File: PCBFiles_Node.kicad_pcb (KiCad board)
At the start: 2 copper layers, 1 part

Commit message: STM32 IC
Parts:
- removed IC**: QFN50P500X500X60-33N-D, SamacSys_Parts:QFN50P500X500X60-33N-D
- added IC1: STM32L432KCU3, SamacSys_Parts:QFN50P500X500X60-33N-D, F.Cu at (125.5, 23.0)

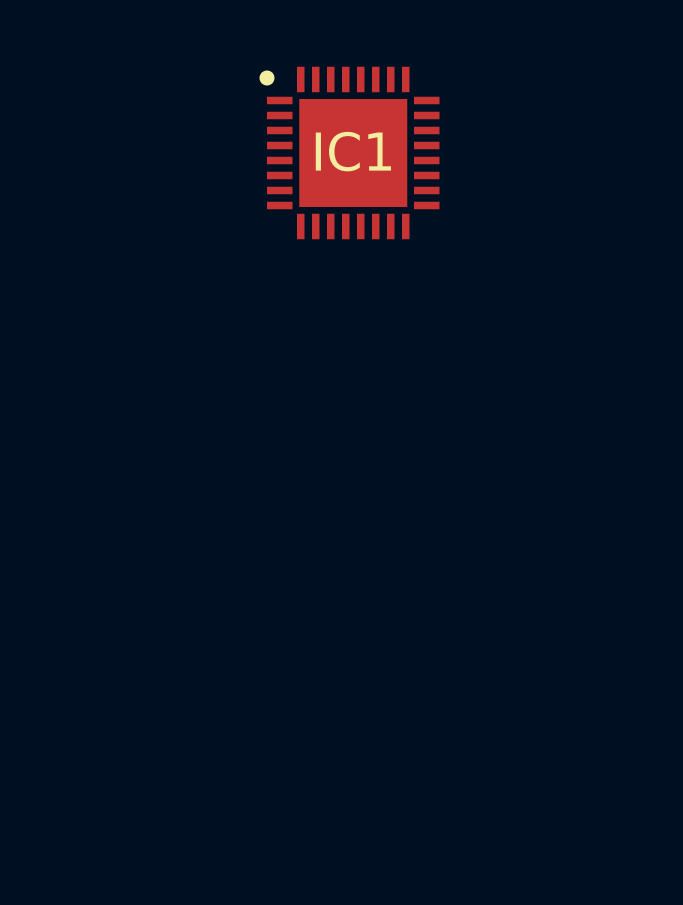
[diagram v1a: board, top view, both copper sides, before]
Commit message: Voltage regulator, Crystal, RFM9x, base settings
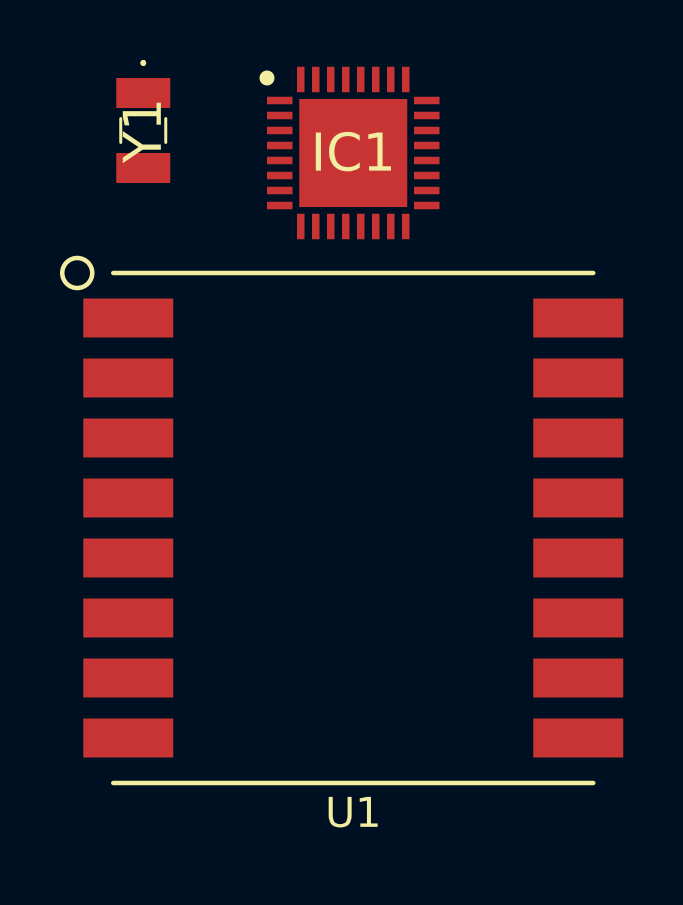
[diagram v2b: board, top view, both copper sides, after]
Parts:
- added U1: RFM9X, LoRa_RFM9x:RFM9X-SMD, F.Cu at (125.5, 35.5)
- added Y1: NX3215SA-32.768K-STD-MUS-2, SamacSys_Parts:NX3215SA32768KSTDMUS2, F.Cu at (118.5, 22.2)
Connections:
- IC1 pad 1: unconnected-(IC1-Pad1) -> +3V3
- IC1 pad 16: unconnected-(IC1-Pad16) -> GND
- IC1 pad 17: unconnected-(IC1-Pad17) -> +3V3
- IC1 pad 19: unconnected-(IC1-Pad19) -> I2C1_SCL
- IC1 pad 2: unconnected-(IC1-Pad2) -> HSE_IN
- IC1 pad 20: unconnected-(IC1-Pad20) -> I2C1_SDA
- IC1 pad 21: unconnected-(IC1-Pad21) -> SPI1_MISO
- IC1 pad 22: unconnected-(IC1-Pad22) -> SPI1_MOSI
- IC1 pad 3: unconnected-(IC1-Pad3) -> HSE_OUT
- IC1 pad 32: unconnected-(IC1-Pad32) -> GND
- IC1 pad 33: unconnected-(IC1-Pad33) -> GND
- IC1 pad 5: unconnected-(IC1-Pad5) -> +3.3VA
- IC1 pad 7: unconnected-(IC1-Pad7) -> SPI1_SCK

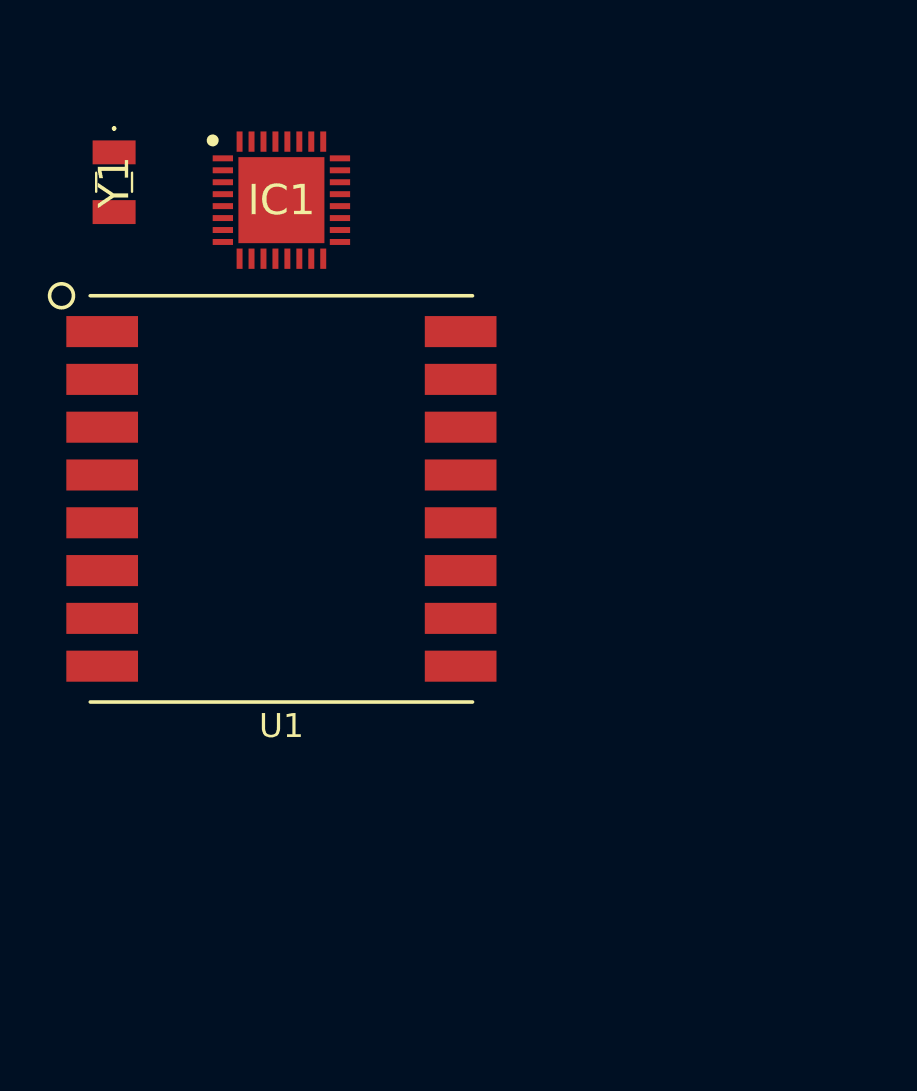
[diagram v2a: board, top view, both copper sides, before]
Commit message: Connectors, MPU Circuit & Pins Schematic Update
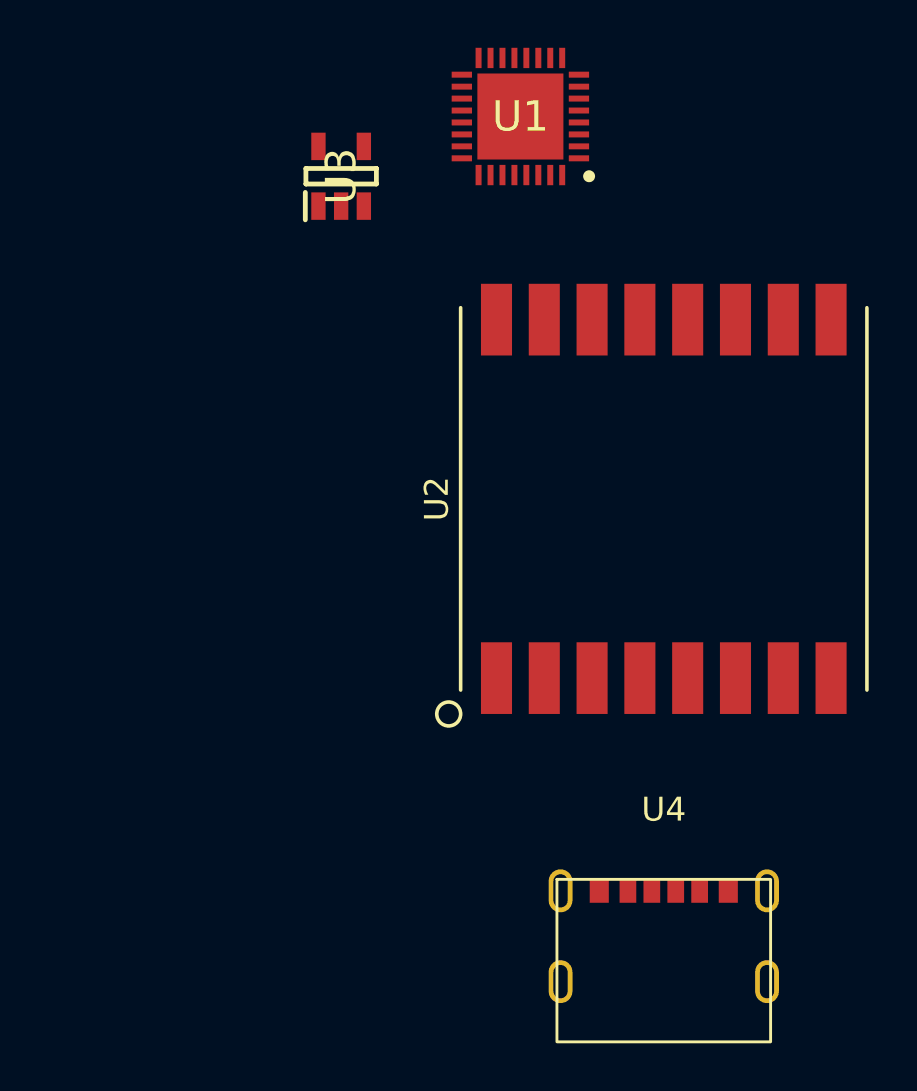
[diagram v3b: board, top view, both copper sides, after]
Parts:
- removed IC1: STM32L432KCU3, SamacSys_Parts:QFN50P500X500X60-33N-D
- removed Y1: NX3215SA-32.768K-STD-MUS-2, SamacSys_Parts:NX3215SA32768KSTDMUS2
- added U2: RFM9X, LoRa_RFM9x:RFM9X-SMD, F.Cu at (141.5, 35.5)
- added U3: STLQ015M33R, SamacSys_Parts:SOT95P280X145-5N, F.Cu at (128.0, 22.0)
- added U4: USB_C_2.0_6PIN, Connector_USB:USB_TYPE_C_2.0_6PIN, F.Cu at (141.5, 49.0)
- U1: value RFM9X -> STM32L432KCU3; footprint LoRa_RFM9x:RFM9X-SMD -> SamacSys_Parts:QFN50P500X500X60-33N-D
- moved U1 18.9 mm to (135.5, 19.5)
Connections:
- net DIO0 renamed V_GAS
- net DIO4 renamed RED_LED
- U1 pad 1: GND -> +3V3
- U1 pad 10: DIO1 -> V_REF_OUT
- U1 pad 12: +3V3 -> RESET_RFM9X
- U1 pad 14: DIO3 -> unconnected-(U1-Pad14)
- U1 pad 15: GND -> unconnected-(U1-Pad15)
- U1 pad 16: /ANT -> GND
- U1 pad 2: SPI1_MISO -> HSE_IN
- U1 pad 3: SPI1_MOSI -> HSE_OUT
- U1 pad 4: SPI1_SCK -> Net-(C1-Pad1)
- U1 pad 5: SPI1_NSS -> +3V3
- U1 pad 6: RESET_RFM9X -> V_REF_IN
- U1 pad 7: DIO5 -> SPI1_SCK
- U1 pad 8: GND -> GREEN_LED
- U1 pad 9: DIO2 -> V_REF_OUT

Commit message: First PCB Design
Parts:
- removed U4: USB_C_2.0_6PIN, Connector_USB:USB_TYPE_C_2.0_6PIN
- added C1: 100n, Capacitor_SMD:C_0402_1005Metric, F.Cu at (124.0, 87.9)
- added C10: 1u, Capacitor_SMD:C_0402_1005Metric, F.Cu at (119.5, 89.7)
- added C11: 10n, Capacitor_SMD:C_0402_1005Metric, F.Cu at (119.0, 88.1)
- added C2: 1u, Capacitor_SMD:C_0402_1005Metric, F.Cu at (124.4, 96.6)
- added C3: 10u, Capacitor_SMD:C_1206_3216Metric, F.Cu at (106.1, 100.2)
- added C4: 100n, Capacitor_SMD:C_0402_1005Metric, F.Cu at (125.6, 96.6)
- added C5: 100n, Capacitor_SMD:C_0402_1005Metric, F.Cu at (126.8, 96.6)
- added C6: 100n, Capacitor_SMD:C_0402_1005Metric, F.Cu at (128.0, 96.6)
- added C7: 10u, Capacitor_SMD:C_1206_3216Metric, F.Cu at (106.7, 87.7)
- added C8: 13p, Capacitor_SMD:C_0402_1005Metric, F.Cu at (114.2, 91.5)
- added C9: 13p, Capacitor_SMD:C_0402_1005Metric, F.Cu at (114.2, 93.6)
- added D1: Green, LED_SMD:LED_0201_0603Metric, F.Cu at (116.5, 96.3)
- added D2: Red, LED_SMD:LED_0201_0603Metric, F.Cu at (120.7, 98.5)
- added H1: MountingHole, MountingHole:MountingHole_2.2mm_M2_Pad_Via, F.Cu at (161.6, 80.4)
- added H2: MountingHole, MountingHole:MountingHole_2.2mm_M2_Pad_Via, F.Cu at (101.6, 101.9)
- added J1: SWD, Connector_PinHeader_2.54mm:PinHeader_2x05_P2.54mm_Vertical_SMD, F.Cu at (133.1, 84.4)
- added J2: SHT31, Connector_PinSocket_2.54mm:PinSocket_1x07_P2.54mm_Vertical, F.Cu at (141.7, 102.8)
- added J3: SPEC Sensor 968-001, Connector_PinHeader_2.54mm:PinHeader_1x08_P2.54mm_Horizontal, B.Cu at (110.1, 97.0)
- added J5: USB_B_Micro, Connector_USB:USB_Micro-B_Molex-105017-0001, F.Cu at (101.7, 94.9)
- added J6: Input, TerminalBlock:TerminalBlock_bornier-2_P5.08mm, B.Cu at (103.0, 85.3)
- added J7: SMA, Connector_Coaxial:SMA_Samtec_SMA-J-P-X-ST-EM1_EdgeMount, F.Cu at (162.3, 100.4)
- added L1: 39n, Inductor_SMD:L_0402_1005Metric, F.Cu at (117.9, 90.2)
- added R1: 10k, Resistor_SMD:R_0402_1005Metric, F.Cu at (121.5, 89.2)
- added R2: 1k, Resistor_SMD:R_0603_1608Metric, F.Cu at (116.5, 99.1)
- added R3: 1k, Resistor_SMD:R_0603_1608Metric, F.Cu at (120.7, 101.2)
- added SW1: SW_Push, Button_Switch_SMD:SW_SPST_B3U-1000P, F.Cu at (123.9, 85.1)
- added U5: USBLC6-2SC6, Package_TO_SOT_SMD:SOT-23-6, F.Cu at (111.0, 101.4)
- added Y1: Q13FC1350000400 32.768kHz, Crystal:Q13FC1350000400, F.Cu at (112.9, 92.6)
- U1: value STM32L432KCU3 -> STM32L432KCUx
- moved U1 76.1 mm to (120.5, 94.1), turned to 0 degrees
- moved U3 73.8 mm to (106.3, 92.5)
- moved U2 57.8 mm to (149.8, 92.7), turned to 0 degrees
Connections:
- net SPI1_NSS renamed SPI3_NSS
- U1 pad 21: SPI1_MISO -> USB_D-
- U1 pad 22: SPI1_MOSI -> USB_D+
- U1 pad 26: unconnected-(U1-Pad26) -> SPI3_SCK
- U1 pad 27: unconnected-(U1-Pad27) -> SPI3_MISO
- U1 pad 28: unconnected-(U1-Pad28) -> SPI3_MOSI
- U1 pad 4: Net-(C1-Pad1) -> NRST
- U1 pad 5: +3V3 -> +3.3VA
- U1 pad 7: SPI1_SCK -> unconnected-(U1-Pad7)
- U2 pad 2: SPI1_MISO -> SPI3_MISO
- U2 pad 3: SPI1_MOSI -> SPI3_MOSI
- U2 pad 4: SPI1_SCK -> SPI3_SCK
- U3 pad 1: +4V -> +5V
- U3 pad 3: +4V -> +5V
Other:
- board outline added: 65.5 x 27 mm

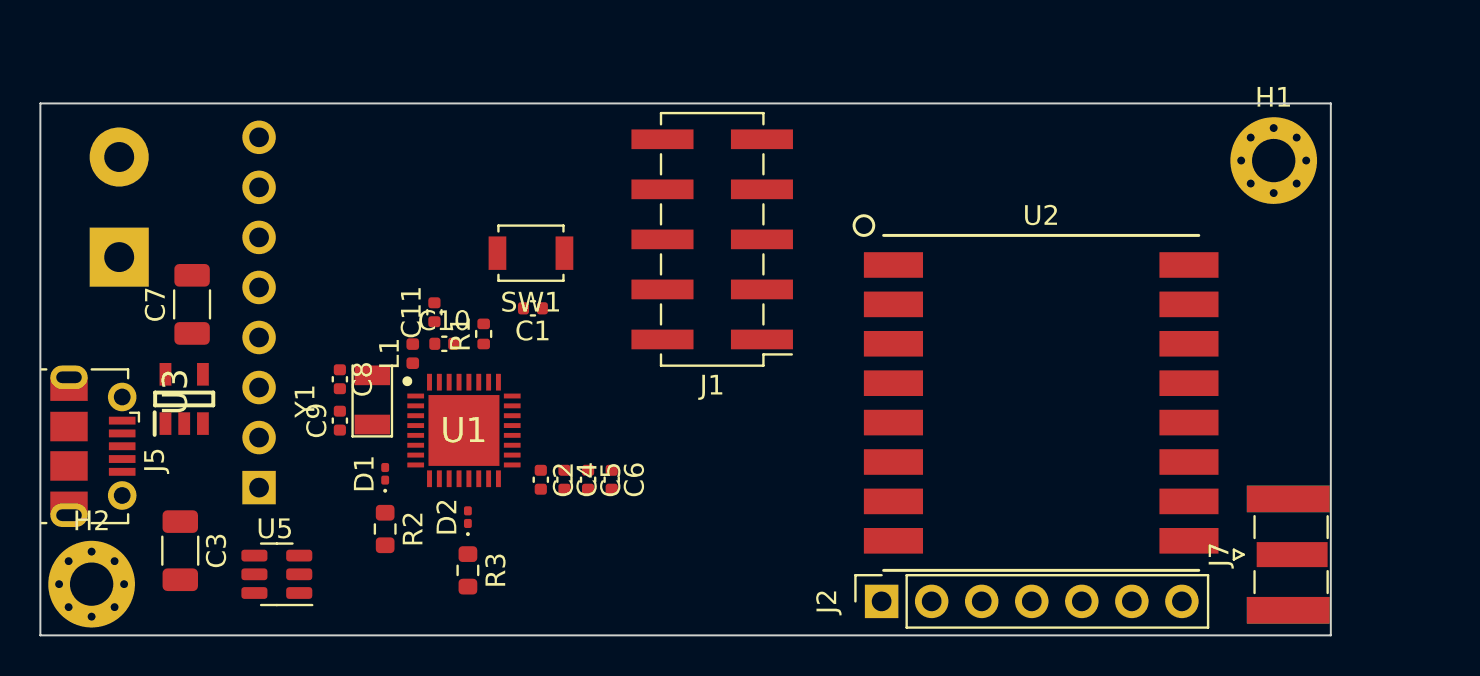
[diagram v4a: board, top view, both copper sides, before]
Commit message: Replaced STM32L432KCU6 for STM32L431RCTx in Schematic and PCB
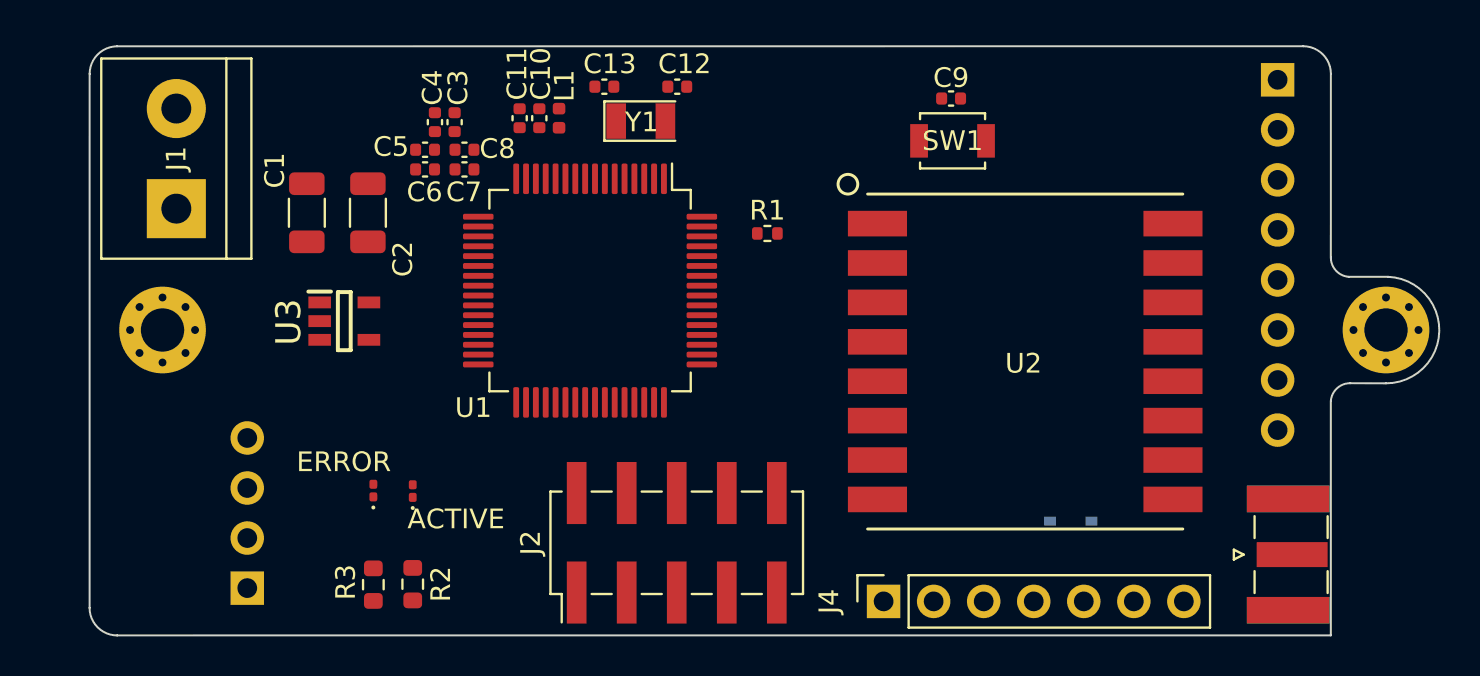
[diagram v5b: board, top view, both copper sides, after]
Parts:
- removed J6: Input, TerminalBlock:TerminalBlock_bornier-2_P5.08mm
- removed U5: USBLC6-2SC6, Package_TO_SOT_SMD:SOT-23-6
- added C12: 13p, Capacitor_SMD:C_0402_1005Metric, F.Cu at (131.3, 76.7)
- added C13: 13p, Capacitor_SMD:C_0402_1005Metric, F.Cu at (127.6, 76.7)
- added ERROR: Red, LED_SMD:LED_0201_0603Metric, F.Cu at (115.9, 97.2)
- added J4: SHT31, Connector_PinSocket_2.54mm:PinSocket_1x07_P2.54mm_Vertical, F.Cu at (141.8, 102.8)
- ACTIVE: renamed from D2; value Red -> Green
- C1: value 100n -> 10u; footprint Capacitor_SMD:C_0402_1005Metric -> Capacitor_SMD:C_1206_3216Metric
- C2: value 1u -> 10u; footprint Capacitor_SMD:C_0402_1005Metric -> Capacitor_SMD:C_1206_3216Metric
- C3: value 10u -> 1u; footprint Capacitor_SMD:C_1206_3216Metric -> Capacitor_SMD:C_0402_1005Metric
- C7: value 10u -> 100n; footprint Capacitor_SMD:C_1206_3216Metric -> Capacitor_SMD:C_0402_1005Metric
- C8, C9: value 13p -> 100n
- D1: value Green -> Schottky; footprint LED_SMD:LED_0201_0603Metric -> Diode_SMD:D_SOD-323; moved to B.Cu
- J1: value SWD -> Input; footprint Connector_PinHeader_2.54mm:PinHeader_2x05_P2.54mm_Vertical_SMD -> TerminalBlock:TerminalBlock_bornier-2_P5.08mm
- J2: value SHT31 -> SWD; footprint Connector_PinSocket_2.54mm:PinSocket_1x07_P2.54mm_Vertical -> Connector_PinHeader_2.54mm:PinHeader_2x05_P2.54mm_Vertical_SMD
- J5: value USB_B_Micro -> USB-TTL; footprint Connector_USB:USB_Micro-B_Molex-105017-0001 -> Connector_PinSocket_2.54mm:PinSocket_1x04_P2.54mm_Horizontal; moved to B.Cu
- U1: value STM32L432KCUx -> STM32L431RCTx; footprint SamacSys_Parts:QFN50P500X500X60-33N-D -> Package_QFP:LQFP-64_10x10mm_P0.5mm
- moved J3 55.7 mm to (161.8, 76.3), turned to 180 degrees
- moved C9 35.1 mm to (145.2, 77.2), turned to 0 degrees
- moved D1 34.9 mm to (151.3, 98.7), turned to 180 degrees
- moved J1 27.2 mm to (105.9, 82.8), turned to 90 degrees
- moved C3 25.8 mm to (120.0, 78.5), turned to 90 degrees
- moved Y1 23.8 mm to (129.4, 75.5), turned to 0 degrees
- moved SW1 22.1 mm to (145.3, 79.4), turned to 0 degrees
- moved C4 19.3 mm to (119.0, 78.5), turned to 90 degrees
- moved C5 18.7 mm to (118.5, 79.8), turned to 180 degrees
- moved C6 18.4 mm to (118.5, 80.8), turned to 180 degrees
- moved C2 16.1 mm to (115.6, 83.0), turned to 90 degrees
- moved C7 15.4 mm to (120.5, 80.8), turned to 0 degrees
- moved R1 15.3 mm to (135.9, 84.1), turned to 0 degrees
- moved L1 14.1 mm to (125.3, 78.2), turned to -90 degrees
- moved H2 13.4 mm to (105.2, 89.0)
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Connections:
- ACTIVE pad 2: RED_LED -> GREEN_LED
- C1 pad 1: NRST -> +5V
- C3 pad 1: +5V -> +3V3
- C8 pad 1: HSE_IN -> +3V3
- C9 pad 1: HSE_OUT -> NRST
- D1 pad 2: GREEN_LED -> +3V3
- J1 pad 1: +3V3 -> +5V
- J1 pad 2: SWDIO -> GND
- J2 pad 2: GND -> SWDIO
- J2 pad 3: I2C1_SCL -> GND
- J2 pad 4: I2C1_SDA -> SWCLK
- J2 pad 5: unconnected-(J2-Pad5) -> GND
- J3 pad 8: +3V3 -> Net-(D1-Pad1)
- J5 pad 1: +5V -> GND
- J5 pad 2: USB_CONN_D- -> LPUART1_TX
- J5 pad 3: USB_CONN_D+ -> LPUART1_RX
- J5 pad 4: unconnected-(J5-Pad4) -> +5V
- R1 pad 1: Net-(R1-Pad1) -> BOOT0
- R2 pad 1: Net-(D1-Pad1) -> Net-(D2-Pad1)
- R3 pad 1: Net-(D2-Pad1) -> Net-(D3-Pad1)
- U1 pad 10: V_REF_OUT -> unconnected-(U1-Pad10)
- U1 pad 11: V_GAS -> unconnected-(U1-Pad11)
- U1 pad 12: RESET_RFM9X -> GND
- U1 pad 13: RED_LED -> +3.3VA
- U1 pad 14: unconnected-(U1-Pad14) -> V_REF_IN
- U1 pad 16: GND -> unconnected-(U1-Pad16)
- U1 pad 17: +3V3 -> V_REF_OUT
- U1 pad 18: SPI3_NSS -> GND
- U1 pad 19: I2C1_SCL -> +3V3
- U1 pad 2: HSE_IN -> unconnected-(U1-Pad2)
- U1 pad 20: I2C1_SDA -> unconnected-(U1-Pad20)
- U1 pad 21: USB_D- -> unconnected-(U1-Pad21)
- U1 pad 22: USB_D+ -> V_GAS
- U1 pad 23: SWDIO -> V_REF_OUT
- U1 pad 24: SWCLK -> unconnected-(U1-Pad24)
- U1 pad 26: SPI3_SCK -> unconnected-(U1-Pad26)
- U1 pad 27: SPI3_MISO -> unconnected-(U1-Pad27)
- U1 pad 28: SPI3_MOSI -> unconnected-(U1-Pad28)
- U1 pad 3: HSE_OUT -> LSE_IN
- U1 pad 31: Net-(R1-Pad1) -> GND
- U1 pad 32: GND -> +3V3
- U1 pad 33: GND -> unconnected-(U1-Pad33)
- U1 pad 4: NRST -> LSE_OUT
- U1 pad 5: +3.3VA -> unconnected-(U1-Pad5)
- U1 pad 6: V_REF_IN -> unconnected-(U1-Pad6)
- U1 pad 7: unconnected-(U1-Pad7) -> NRST
- U1 pad 8: GREEN_LED -> LPUART1_RX
- U1 pad 9: V_REF_OUT -> LPUART1_TX
- U2 pad 10: DIO1 -> unconnected-(U2-Pad10)
- U2 pad 11: DIO0 -> unconnected-(U2-Pad11)
- U2 pad 13: DIO4 -> unconnected-(U2-Pad13)
- U2 pad 14: DIO3 -> unconnected-(U2-Pad14)
- U2 pad 7: DIO5 -> unconnected-(U2-Pad7)
- U2 pad 9: DIO2 -> unconnected-(U2-Pad9)
- Y1 pad 1: HSE_OUT -> LSE_OUT
- Y1 pad 2: HSE_IN -> LSE_IN
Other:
- board size 65.5 x 27 mm -> 68.5 x 29.9 mm
- board text added: "+5V"
- board text added: "GND"
- board text added: "RX"
- board text added: "TX"
